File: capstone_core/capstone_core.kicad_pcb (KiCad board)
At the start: 4 copper layers, 75 x 80 mm, 22 parts, among them J1 Conn_02x20_Odd_Even, J2 2x5 CONN DSUB-PCB, J3 2x5 CONN DSUB-PCB, J4 Conn_01x02_Socket, J5 Conn_01x02_Socket, J6 Conn_01x02_Socket, U1 ZED F9P GNSS & RTK Module

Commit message: Core PCB. Revision 1.0
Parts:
- removed J6: Conn_01x02_Socket, Capstone Footprints:1x2_CONN_SD-43650-010_02_MOL
- added C1: 22uF/35V, Capacitor_SMD:C_0805_2012Metric_Pad1.18x1.45mm_HandSolder, F.Cu at (173.7, 108.4)
- added C10: 100uF/16V, Capstone Footprints:CAP_100uF_16V_16SEPC100M_TSS, F.Cu at (171.6, 84.5)
- added C11: 0.1uF/10V, Capacitor_SMD:C_0603_1608Metric_Pad1.08x0.95mm_HandSolder, F.Cu at (172.1, 116.3)
- added C12: 680uF/35V, Capstone Footprints:CAP_680uF_35V_UHW1V681MPD6, F.Cu at (140.9, 133.4)
- added C13: 22uF/10V, Capacitor_SMD:C_0805_2012Metric_Pad1.18x1.45mm_HandSolder, F.Cu at (174.5, 136.7)
- added C14: 1uF/35V, Capacitor_SMD:C_0603_1608Metric_Pad1.08x0.95mm_HandSolder, F.Cu at (152.7, 110.6)
- added C15: 22uF/10V, Capacitor_SMD:C_0805_2012Metric_Pad1.18x1.45mm_HandSolder, F.Cu at (172.4, 136.7)
- added C16: 10nF/50V, Capacitor_SMD:C_0603_1608Metric_Pad1.08x0.95mm_HandSolder, F.Cu at (155.3, 108.2)
- added C17: 22uF/10V, Capacitor_SMD:C_0805_2012Metric_Pad1.18x1.45mm_HandSolder, F.Cu at (170.4, 136.7)
- added C18: 22uF/10V, Capacitor_SMD:C_0805_2012Metric_Pad1.18x1.45mm_HandSolder, F.Cu at (168.4, 136.7)
- added C19: 22uF/10V, Capacitor_SMD:C_0805_2012Metric_Pad1.18x1.45mm_HandSolder, F.Cu at (166.3, 136.7)
- added C2: 22uF/35V, Capacitor_SMD:C_0805_2012Metric_Pad1.18x1.45mm_HandSolder, F.Cu at (173.7, 106.3)
- added C20: 22uF/10V, Capacitor_SMD:C_0805_2012Metric_Pad1.18x1.45mm_HandSolder, F.Cu at (164.3, 136.7)
- added C21: 2.2uF/6.3V, Capacitor_SMD:C_0603_1608Metric_Pad1.08x0.95mm_HandSolder, F.Cu at (150.2, 107.2)
- added C22: 15pF/50V, Capacitor_SMD:C_0603_1608Metric_Pad1.08x0.95mm_HandSolder, F.Cu at (178.2, 120.0)
- added C23: 330uF/35V, Capstone Footprints:CAP_330uF_35V_UCL1V331MNL1GS-L, F.Cu at (153.8, 135.3)
- added C24: 220uF/10V, Capstone Footprints:CAP_100uF_16V_16SEPC100M_TSS, F.Cu at (180.4, 134.5)
- added C25: 680uF/35V, Capstone Footprints:CAP_680uF_35V_UHW1V681MPD6, F.Cu at (138.2, 87.0)
- added C26: 1uF/35V, Capacitor_SMD:C_0603_1608Metric_Pad1.08x0.95mm_HandSolder, F.Cu at (154.3, 116.5)
- added C27: 1uF/35V, Capacitor_SMD:C_0603_1608Metric_Pad1.08x0.95mm_HandSolder, F.Cu at (151.0, 64.6)
- added C28: 10nF/50V, Capacitor_SMD:C_0603_1608Metric_Pad1.08x0.95mm_HandSolder, F.Cu at (156.9, 113.1)
- added C29: 10nF/50V, Capacitor_SMD:C_0603_1608Metric_Pad1.08x0.95mm_HandSolder, F.Cu at (153.6, 61.2)
- added C3: 1uF/35V, Capacitor_SMD:C_0805_2012Metric_Pad1.18x1.45mm_HandSolder, F.Cu at (173.7, 104.3)
- added C30: 330uF/35V, Capstone Footprints:CAP_330uF_35V_UCL1V331MNL1GS-L, F.Cu at (156.4, 73.9)
- added C31: 4.7uF/6.3V, Capacitor_SMD:C_0603_1608Metric_Pad1.08x0.95mm_HandSolder, F.Cu at (151.8, 113.1)
- added C32: 4.7uF/6.3V, Capacitor_SMD:C_0603_1608Metric_Pad1.08x0.95mm_HandSolder, F.Cu at (148.6, 61.2)
- added C33: 1uF/35V, Capacitor_SMD:C_0603_1608Metric_Pad1.08x0.95mm_HandSolder, F.Cu at (169.8, 112.2)
- added C4: 10nF/50V, Capacitor_SMD:C_0603_1608Metric_Pad1.08x0.95mm_HandSolder, F.Cu at (169.8, 100.9)
- added C5: 10uF/25V, Capacitor_SMD:C_0805_2012Metric_Pad1.18x1.45mm_HandSolder, F.Cu at (176.3, 118.4)
- added C6: 10uF/25V, Capacitor_SMD:C_0805_2012Metric_Pad1.18x1.45mm_HandSolder, F.Cu at (163.9, 118.2)
- added C7: 1uF/35V, Capacitor_SMD:C_0603_1608Metric_Pad1.08x0.95mm_HandSolder, F.Cu at (169.8, 113.8)
- added C8: 1uF/35V, Capacitor_SMD:C_0603_1608Metric_Pad1.08x0.95mm_HandSolder, F.Cu at (174.4, 118.4)
- added C9: 1uF/35V, Capacitor_SMD:C_0603_1608Metric_Pad1.08x0.95mm_HandSolder, F.Cu at (165.7, 117.9)
- added D1: 50V/3A, Diode_SMD:D_SMC_Handsoldering, F.Cu at (161.9, 102.6)
- added D2: 50V/3A, Diode_SMD:D_SMC_Handsoldering, F.Cu at (131.1, 123.4)
- added D3: 50V/3A, Diode_SMD:D_SMC_Handsoldering, F.Cu at (145.9, 88.0)
- added H4: MountingHole, MountingHole:MountingHole_2.7mm, F.Cu at (186.4, 140.7)
- added L1: 33uH, Capstone Footprints:IND_33uH_3A_CDRH127NP-330MC, F.Cu at (162.9, 92.2)
- added L2: 6.8uH, Capstone Footprints:IND_6.8uH_CB_DRA127, F.Cu at (168.9, 127.4)
- added L3: 33uH, Capstone Footprints:IND_33uH_3A_CDRH127NP-330MC, F.Cu at (145.2, 122.7)
- added L4: 33uH, Capstone Footprints:IND_33uH_3A_CDRH127NP-330MC, F.Cu at (144.4, 74.0)
- added R1: 47k, Resistor_SMD:R_0603_1608Metric_Pad0.98x0.95mm_HandSolder, F.Cu at (178.3, 104.1)
- added R2: 47k, Resistor_SMD:R_0603_1608Metric_Pad0.98x0.95mm_HandSolder, F.Cu at (169.8, 110.6)
- added R3: 100k, Resistor_SMD:R_0603_1608Metric_Pad0.98x0.95mm_HandSolder, F.Cu at (179.7, 120.5)
- added R4: 23.2k, Resistor_SMD:R_0603_1608Metric_Pad0.98x0.95mm_HandSolder, F.Cu at (179.7, 117.1)
- added R5: 4.9k, Resistor_SMD:R_0603_1608Metric_Pad0.98x0.95mm_HandSolder, F.Cu at (178.2, 123.4)
- added RV1: 2k, Capstone Footprints:POT_2k_PV36W202C01B00, F.Cu at (181.5, 112.4)
- added TP12: TestPoint, Capstone Footprints:testpoint_1.0mm_hole, F.Cu at (163.6, 70.9)
- added TP13: TestPoint, Capstone Footprints:testpoint_1.0mm_hole, F.Cu at (127.8, 60.0)
- added TP14: TestPoint, Capstone Footprints:testpoint_1.0mm_hole, F.Cu at (160.9, 145.6)
- added TP15: TestPoint, Capstone Footprints:testpoint_1.0mm_hole, F.Cu at (178.8, 145.9)
- added U3: LM2676SX-12/NOPB, Capstone Footprints:LM2676SX-12-L, F.Cu at (174.9, 93.7)
- added U4: LM62460QRPHRQ1, Capstone Footprints:LM62460QRPHRQ1, F.Cu at (168.9, 117.2)
- added U5: LM2596S-5.0, Capstone Footprints:LM2596S-5, F.Cu at (129.8, 136.1)
- added U6: LP2985-18DBVR, Capstone Footprints:LP2985-18DBVR, F.Cu at (152.8, 107.6)
- added U7: LM2596S-5.0, Capstone Footprints:LM2596S-5, F.Cu at (129.1, 77.5)
- added U8: LP2985-33DBVR, Capstone Footprints:LP2985-33DBVR, F.Cu at (154.3, 113.6)
- added U9: LP2985-33DBVR, Capstone Footprints:LP2985-33DBVR, F.Cu at (151.1, 61.6)
- H1, H2, H3: footprint MountingHole:MountingHole_2.5mm -> MountingHole:MountingHole_2.7mm
- J1: footprint Capstone Footprints:2x20_CONN_3020-40-0100-00_CNC -> Capstone Footprints:RPI_Hat_B+
- TP1, TP10, TP11, TP2, TP3, TP5, TP6, TP7, TP8, TP9: footprint TestPoint:TestPoint_THTPad_D1.0mm_Drill0.5mm -> Capstone Footprints:testpoint_1.0mm_hole
- TP4: value TestPoint -> +LBW_3V3; footprint TestPoint:TestPoint_THTPad_D1.0mm_Drill0.5mm -> Capstone Footprints:testpoint_1.0mm_hole
- U1: value ZED F9P GNSS & RTK Module -> ~; footprint Capstone Footprints:ZED-F9P -> Capstone Footprints:IMU_Breakout_Module
- U2: value ~ -> ZED F9P GNSS & RTK Module; footprint Capstone Footprints:IMU_Breakout_Module -> Capstone Footprints:ZED-F9P; moved to B.Cu
- moved J5 116.8 mm to (171.7, 77.2), turned to 180 degrees
- moved J4 113.6 mm to (171.6, 70.6), turned to 180 degrees
- moved H3 101.2 mm to (186.4, 82.7)
- moved TP4 91.9 mm to (125.8, 71.1)
- moved J1 89.4 mm to (186.3, 111.7), turned to -90 degrees
- moved TP9 82.8 mm to (144.9, 60.1)
- moved TP5 72.0 mm to (157.8, 59.4)
- moved TP7 60.4 mm to (145.5, 107.8)
- moved TP6 58.7 mm to (145.9, 117.4)
- moved TP11 58.5 mm to (150.8, 106.4)
- moved TP10 55.6 mm to (180.3, 68.7)
- moved TP8 53.7 mm to (180.1, 75.4)
- moved U2 48.5 mm to (141.6, 123.9), turned to 0 degrees
- moved TP2 45.6 mm to (157.4, 128.6)
- moved TP1 36.6 mm to (181.2, 83.6)
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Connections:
- J1 pad 2: unconnected-(J1-Pin_2-Pad2) -> +PI_5V
- J1 pad 4: unconnected-(J1-Pin_4-Pad4) -> +PI_5V
- J5 pad 1: +PI_5V -> +12V
- U1 pad 1: GND -> +3V3
- U1 pad 2: unconnected-(U1-3V3-Pad2) -> +1V8
- U1 pad 3: SCL -> GND
- U1 pad 4: SDA -> unconnected-(U1-NC-Pad4)
- U1 pad 5: unconnected-(U1-FENCE-Pad5) -> SDA
- U1 pad 6: RTK -> SCL
- U2 pad 1: +3V3 -> GND
- U2 pad 2: +1V8 -> unconnected-(U2-3V3-Pad2)
- U2 pad 3: GND -> SCL
- U2 pad 4: unconnected-(U2-NC-Pad4) -> SDA
- U2 pad 5: SDA -> unconnected-(U2-FENCE-Pad5)
- U2 pad 6: SCL -> RTK
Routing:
- net SCL: track 0.00 -> 193.3 mm
- net SDA: track 0.00 -> 180.7 mm
- net GPIO4: track 0.00 -> 93.4 mm
- net GPIO18: track 0.00 -> 85.4 mm
- net RTK: track 0.00 -> 71.8 mm
- net GPIO5: track 0.00 -> 67.8 mm
- net +CORE_5V: track 0.00 -> 64.4 mm
- net PPS: track 0.00 -> 63.5 mm
- net +12V: track 0.00 -> 61.8 mm
- net GPIO20: track 0.00 -> 59.6 mm
- net GPIO9: track 0.00 -> 59.5 mm, vias 0 -> 1
- net +PI_5V: track 0.00 -> 52.6 mm, vias 0 -> 2
- net GPIO8: track 0.00 -> 52.0 mm, vias 0 -> 1
- net RTK_RX: track 0.00 -> 47.6 mm
- net +LBW_5V: track 0.00 -> 47.1 mm
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- added copper zone on F.Cu, net +12V
- added copper zone on F.Cu, net +1V8
- added copper zone on F.Cu, net +3V3
- added copper zone on F.Cu, net +CORE_5V
- added copper zone on F.Cu, net +LBW_3V3
- added copper zone on F.Cu, net +LBW_5V
- added copper zone on F.Cu, net +PI_5V
- added copper zone on F.Cu, net +V_BATT
- added copper zone on In2.Cu, net +V_BATT
- added copper zone on F.Cu, net GND
- added copper zone on In1.Cu, net GND
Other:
- board size 75 x 80 mm -> 71 x 90 mm
- board text added: "EG499/CS414 Core PCB Rev 1.0"
- board text added: "Interdisciplinary Capstone 2025-26"
- board text added: "SNHU"
- board text removed: "+"
- board text removed: "+12V"
- board text removed: "-"
- board text removed: "1"
- board text removed: "Battery"
- board text removed: "Pi +5V"

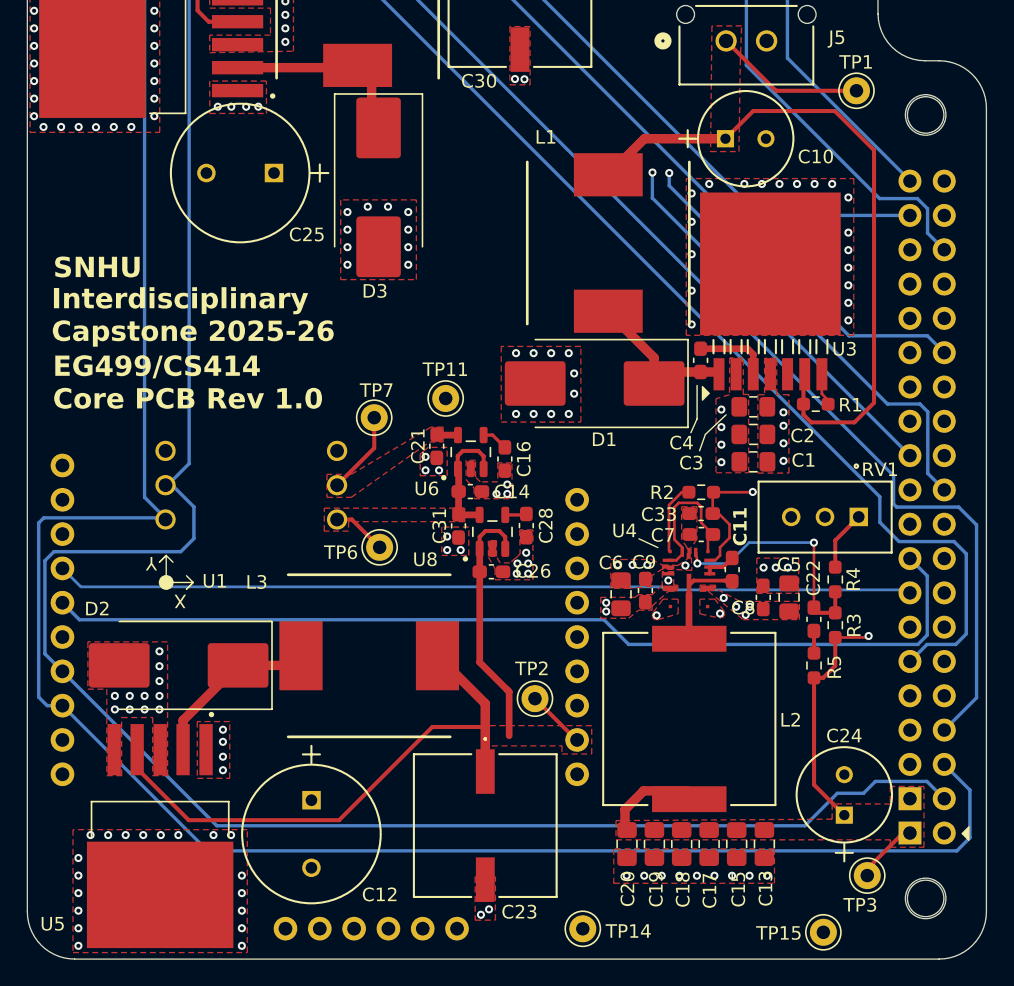
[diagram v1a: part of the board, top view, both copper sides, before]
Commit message: Added 3D models, changed C12 and C25 to shorter capacitor. Fixed library paths to be relative to KiCad project directory
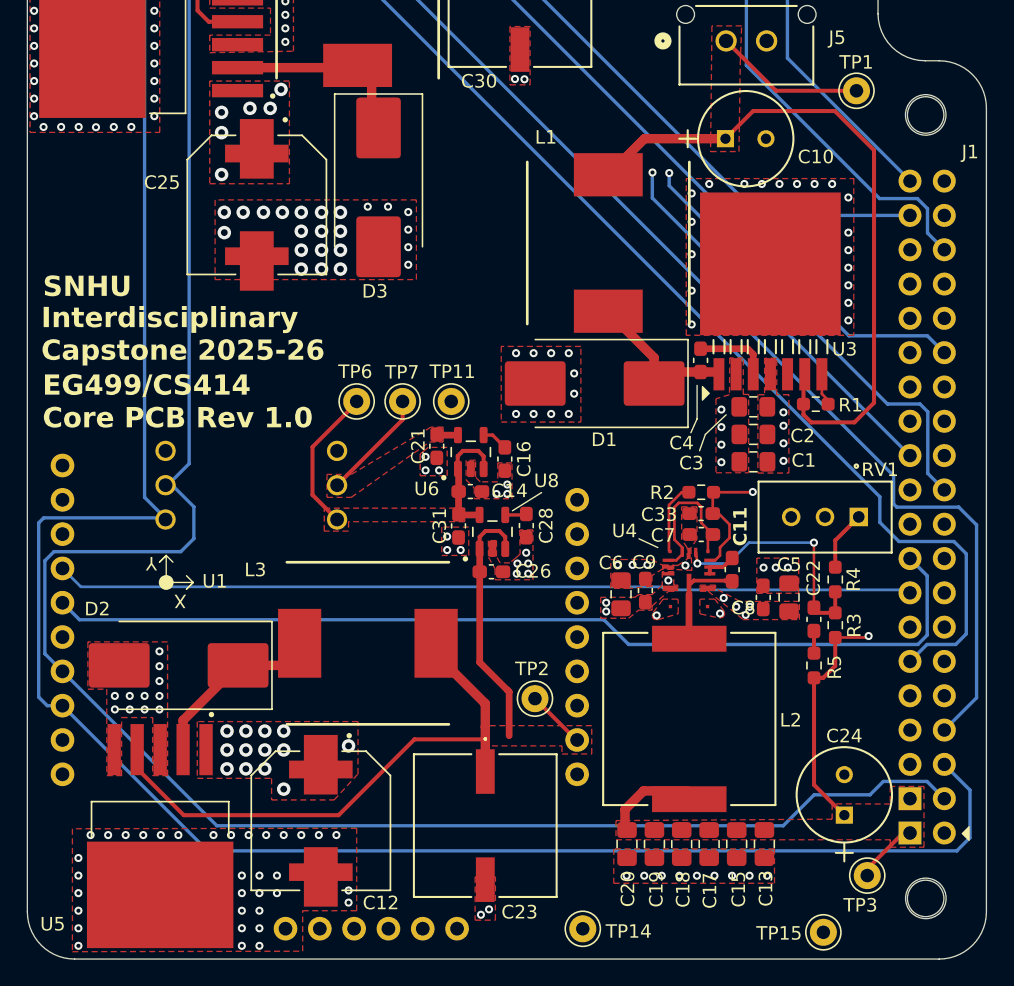
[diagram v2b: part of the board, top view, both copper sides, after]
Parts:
- C12, C25: footprint Capstone Footprints:CAP_680uF_35V_UHW1V681MPD6 -> Capstone Footprints:CAP_680uF_35V_EEHZS1V681UV
- J1: footprint Capstone Footprints:RPI_Hat_B+ -> Capstone Footprints:PI_Connector
- U4: value LM62460QRPHRQ1 -> RPH0016A
- U6: value LP2985-18DBVR -> LP2985-33DBVR
- U8, U9: value LP2985-33DBVR -> LP2985-18DBVR
- moved J1 29.0 mm to (186.4, 82.7)
- moved U2 17.4 mm to (145.4, 140.9)
- moved TP6 10.9 mm to (144.2, 106.6)
- moved C25 2.68 mm to (136.9, 89.3), turned to -90 degrees
- moved TP7 2.42 mm to (147.6, 106.6)
- moved C12 1.68 mm to (141.6, 134.9)
- moved L3 0.93 mm to (145.1, 121.8)
- moved TP11 0.47 mm to (151.2, 106.6)
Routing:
- net +3V3: track 13.0 -> 19.9 mm
- net +1V8: track 7.73 -> 9.80 mm
- net +CORE_5V: track 64.4 -> 65.6 mm
- net /CORE_5V_SW: track 12.9 -> 13.8 mm
- net GND: vias 148 -> 176
- net +V_BATT: vias 19 -> 30
